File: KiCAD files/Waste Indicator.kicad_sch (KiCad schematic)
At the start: 15 parts, among them J101 USB4500-03-0-A, J102 Conn_01x08_Socket, SW101 430172085816, U101 ESP32-S2-MINI-1, U102 AMS1117-3.3

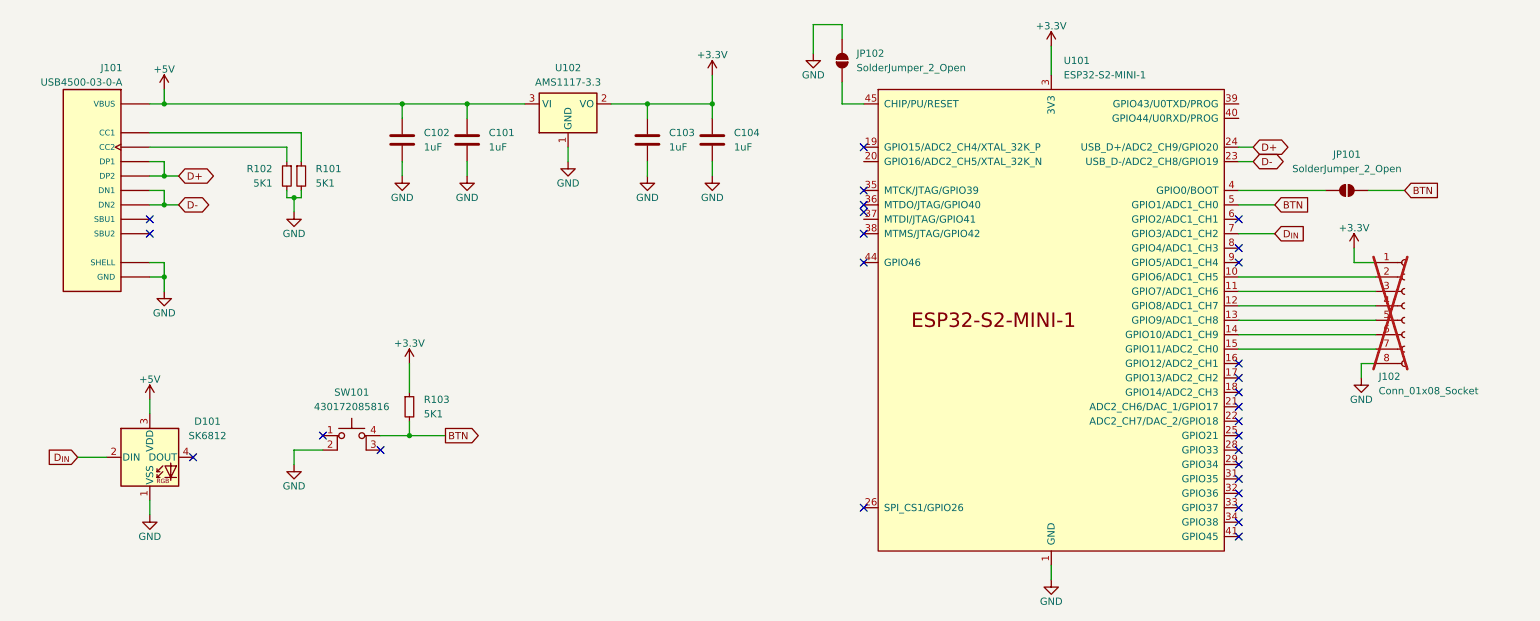
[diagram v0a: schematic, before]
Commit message: Fixed PCB to V1.0
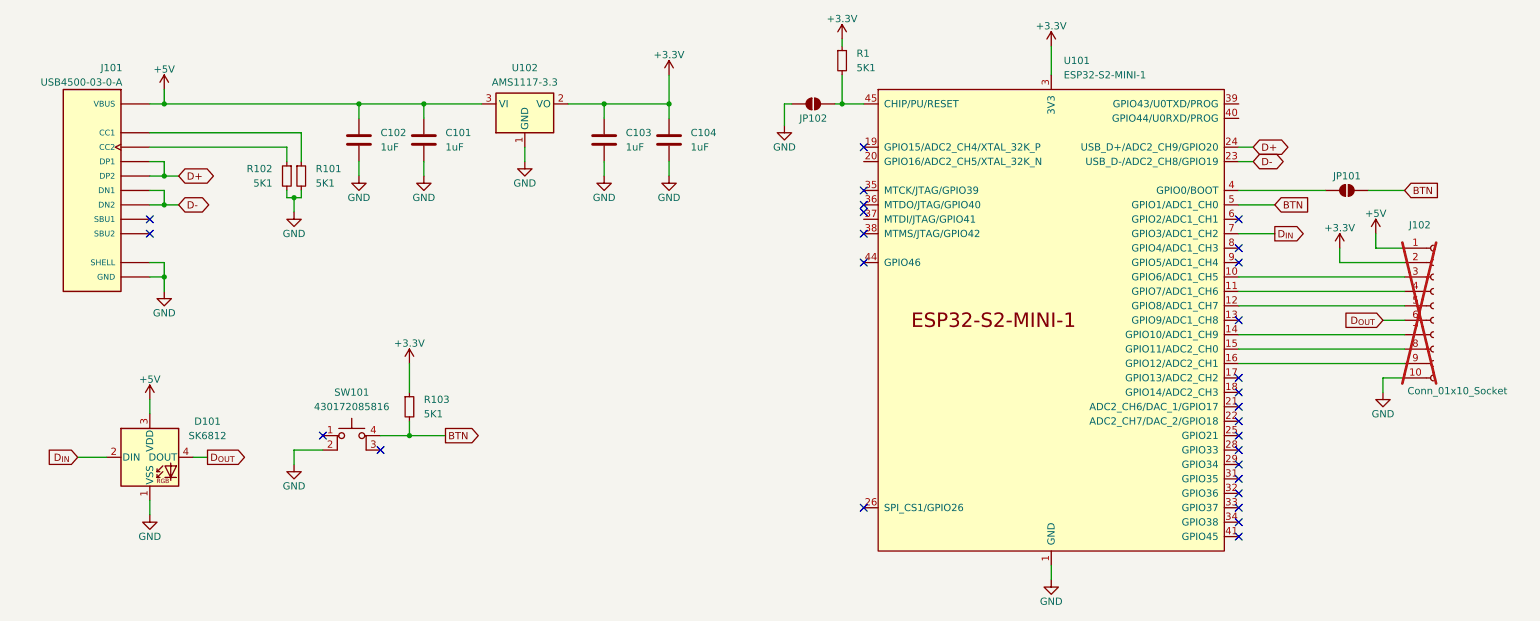
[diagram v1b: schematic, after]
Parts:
- added R1: 5K1, Resistor_SMD:R_0603_1608Metric, symbol .NIT_Resistors:R_0603__5K1
- J102: value Conn_01x08_Socket -> Conn_01x10_Socket; footprint Connector_PinHeader_2.54mm:PinHeader_1x08_P2.54mm_Vertical -> Connector_PinHeader_2.54mm:PinHeader_1x10_P2.54mm_Vertical; symbol Connector:Conn_01x08_Socket -> Connector:Conn_01x10_Socket
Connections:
- net +3.3V: now also J102.2 (Pin_2), R1.1; no longer J102.1 (Pin_1)
- net +5V: now also J102.1 (Pin_1)
- net GND: now also J102.10 (Pin_10); no longer J102.8 (Pin_8)
- net at U101.10 (GPIO6/ADC1_CH5): now also J102.3 (Pin_3); no longer J102.2 (Pin_2)
- net at U101.11 (GPIO7/ADC1_CH6): now also J102.4 (Pin_4); no longer J102.3 (Pin_3)
- net at U101.12 (GPIO8/ADC1_CH7): now also J102.5 (Pin_5); no longer J102.4 (Pin_4)
- net at U101.13 (GPIO9/ADC1_CH8): no longer J102.5 (Pin_5)
- net at U101.14 (GPIO10/ADC1_CH9): now also J102.7 (Pin_7); no longer J102.6 (Pin_6)
- net at U101.15 (GPIO11/ADC2_CH0): now also J102.8 (Pin_8); no longer J102.7 (Pin_7)
- net D_{OUT}: now reaches D101.4 (DOUT)
- net D_{OUT}: now also J102.6 (Pin_6)
- net at JP102.1 (A), U101.45 (CHIP/PU/RESET): now also R1.2
- net at U101.16 (GPIO12/ADC2_CH1): now also J102.9 (Pin_9)
- no-connect marks 28 -> 27
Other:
- moved on the sheet: C101, C102, C103, C104, JP102, U102
